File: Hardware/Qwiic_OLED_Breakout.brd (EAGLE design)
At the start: 27.3 x 29.7 mm, 45 parts, among them J1 QWIIC_RIGHT_ANGLE, J2 QWIIC_RIGHT_ANGLE

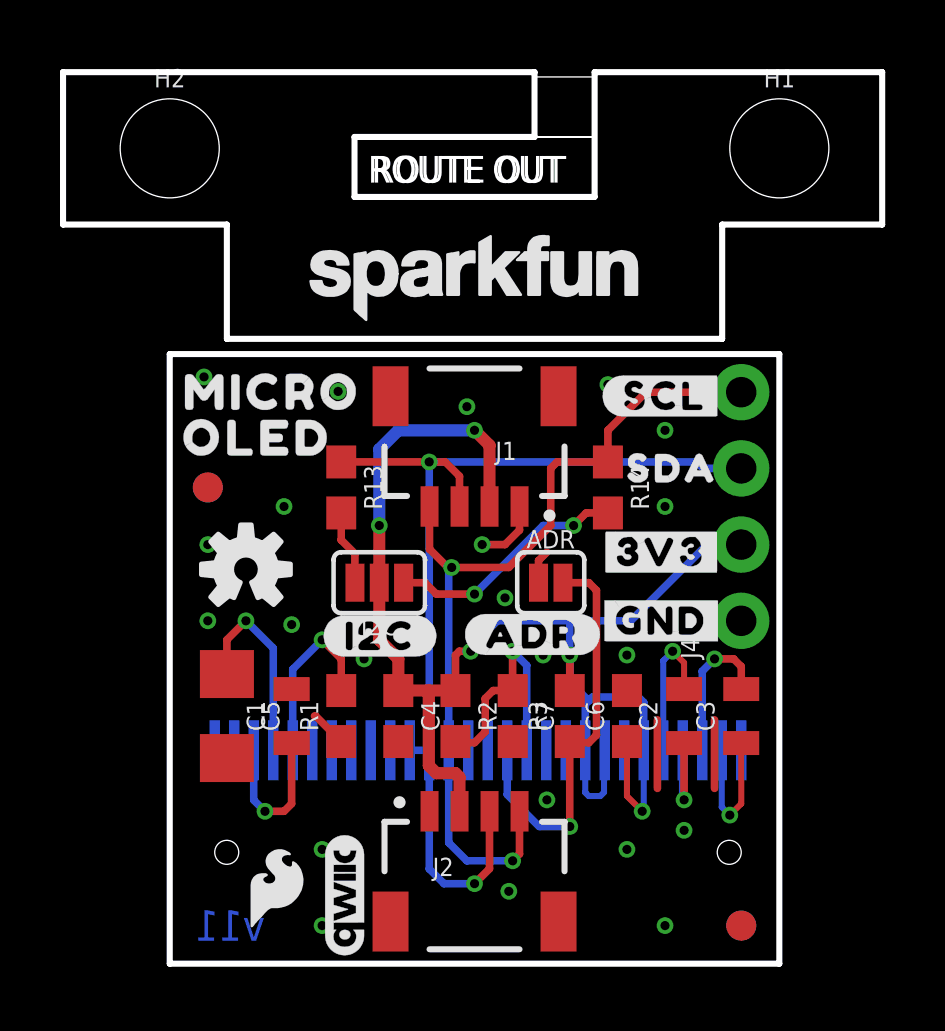
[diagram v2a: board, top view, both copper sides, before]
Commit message: Updates the isolate, replaces the main OLED part, adds some polygons
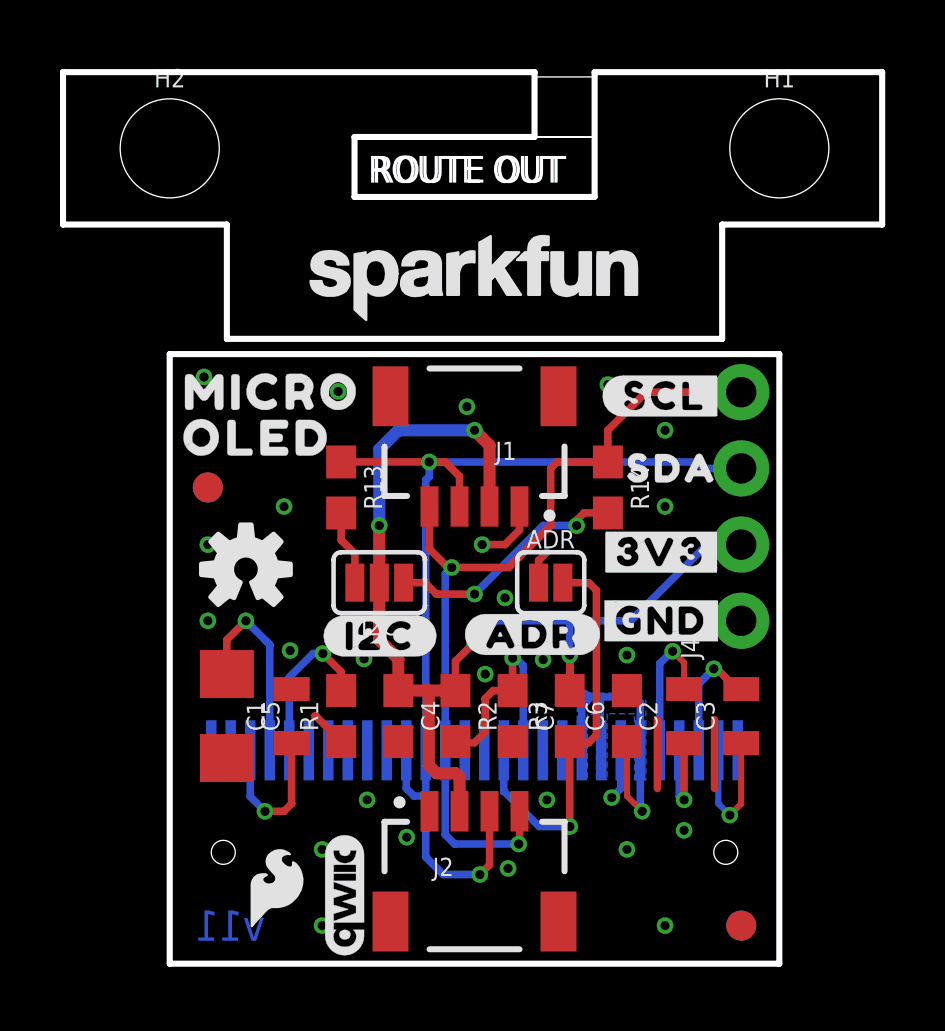
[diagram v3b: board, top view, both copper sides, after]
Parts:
- moved OLED1 8.89 mm to (10.2, 7.11)
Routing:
- net GND: track 9.18 -> 10.9 mm, vias 22 -> 26
- net D1/SDA/PICO: track 34.2 -> 35.2 mm
- net C2N: track 4.96 -> 4.12 mm
- net IREF: track 6.04 -> 5.37 mm
- net D0/SCL/SCK: track 29.6 -> 28.9 mm
- added copper zone on layer 16, net VDD

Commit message: Moves Ordering Instructions
* Updates notes in schematics
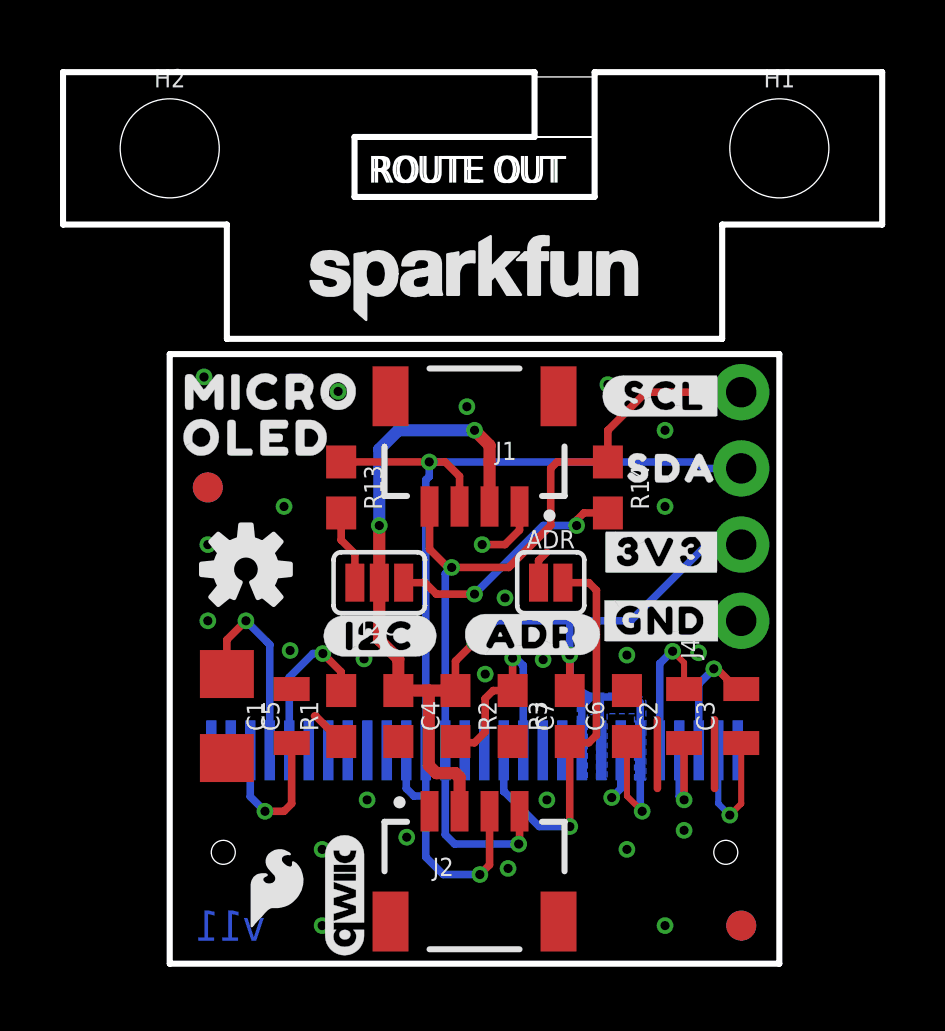
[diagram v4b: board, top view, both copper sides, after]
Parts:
- moved LOGO6 3.81 mm to (34.3, 47.0)
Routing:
- net GND: vias 26 -> 27
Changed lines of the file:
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@@
 <layer number="45" name="Holes" color="7" fill="1" visible="yes" active="yes"/>
 <layer number="46" name="Milling" color="3" fill="1" visible="no" active="yes"/>
-<layer number="47" name="Measures" color="7" fill="1" visible="no" active="yes"/>
+<layer number="47" name="Measures" color="7" fill="1" visible="yes" active="yes"/>
 <layer number="48" name="Document" color="7" fill="1" visible="no" active="yes"/>
 <layer number="49" name="Reference" color="13" fill="1" visible="yes" active="yes"/>
 <layer number="50" name="dxf" color="7" fill="1" visible="no" active="no"/>
 <layer number="51" name="tDocu" color="6" fill="1" visible="yes" active="yes"/>
-<layer number="52" name="bDocu" color="7" fill="1" visible="no" active="yes"/>
+<layer number="52" name="bDocu" color="7" fill="1" visible="yes" active="yes"/>
 <layer number="53" name="tGND_GNDA" color="7" fill="1" visible="no" active="no"/>
 <layer number="54" name="bGND_GNDA" color="7" fill="1" visible="no" active="no"/>
@@
 <dimension x1="10.16" y1="5.08" x2="0" y2="5.08" x3="5.08" y3="-5.08" textsize="1.778" textratio="12" layer="47" unit="inch"/>
 <text x="-26.67" y="-6.35" size="1.778" layer="47" font="vector" ratio="12">Units in Inches</text>
-<text x="31.75" y="34.29" size="1.778" layer="51" font="vector" ratio="12">Two Layer Board</text>
-<text x="31.75" y="31.75" size="1.778" layer="51" font="vector" ratio="12">Red Soldermask</text>
-<text x="31.75" y="29.21" size="1.778" layer="51" font="vector" ratio="12">White Silkscreen</text>
-<text x="31.75" y="26.67" size="1.778" layer="51" font="vector" ratio="12">1.6mm Thickness</text>
-<text x="31.75" y="24.13" size="1.778" layer="51" font="vector" ratio="12">Lead-Free HASL</text>
+<text x="35.56" y="34.29" size="1.778" layer="51" font="vector" ratio="12">Two Layer Board</text>
+<text x="35.56" y="31.75" size="1.778" layer="51" font="vector" ratio="12">Red Soldermask</text>
+<text x="35.56" y="29.21" size="1.778" layer="51" font="vector" ratio="12">White Silkscreen</text>
+<text x="35.56" y="26.67" size="1.778" layer="51" font="vector" ratio="12">1.6mm Thickness</text>
+<text x="35.56" y="24.13" size="1.778" layer="51" font="vector" ratio="12">Lead-Free HASL</text>
 <dimension x1="0" y1="27.178" x2="20.32" y2="27.178" x3="10.16" y3="34.29" textsize="1.778" textratio="15" layer="47" unit="inch"/>
 <dimension x1="20.32" y1="0" x2="20.32" y2="11.43" x3="26.67" y3="5.715" textsize="1.778" textratio="15" layer="47" unit="inch"/>
@@
 <element name="LOGO2" library="SparkFun-Aesthetics" package="SFE_LOGO_NAME_.1" value="SFE_LOGO_NAME.1_INCH" x="10.16" y="22.86" smashed="yes"/>
 <element name="LOGO4" library="SparkFun-Aesthetics" package="SFE_LOGO_NAME_.1" value="SFE_LOGO_NAME.1_INCH" x="6.604" y="18.415" smashed="yes" rot="MR0"/>
-<element name="LOGO6" library="SparkFun-Aesthetics" package="ORDERING_INSTRUCTIONS" value="SPECIAL_INSTRUCTIONS-ORDERING" x="30.48" y="46.99" smashed="yes"/>
+<element name="LOGO6" library="SparkFun-Aesthetics" package="ORDERING_INSTRUCTIONS" value="SPECIAL_INSTRUCTIONS-ORDERING" x="34.29" y="46.99" smashed="yes"/>
 <element name="U$15" library="SparkFun-Aesthetics" package="SFE_LOGO_FLAME_.1" value="" x="3.556" y="2.54" smashed="yes"/>
 <element name="J4" library="SparkFun-Connectors" package="1X04_NO_SILK" value="" x="19.05" y="11.43" smashed="yes" rot="R90">
@@
 <via x="7.8994" y="4.2164" extent="1-16" drill="0.3048"/>
 <via x="10.5156" y="9.652" extent="1-16" drill="0.3048"/>
+<via x="17.6276" y="10.3632" extent="1-16" drill="0.3048"/>
 </signal>
 <signal name="VDD">

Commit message: Adds a single via
* Gets judicious with the text in the schematic
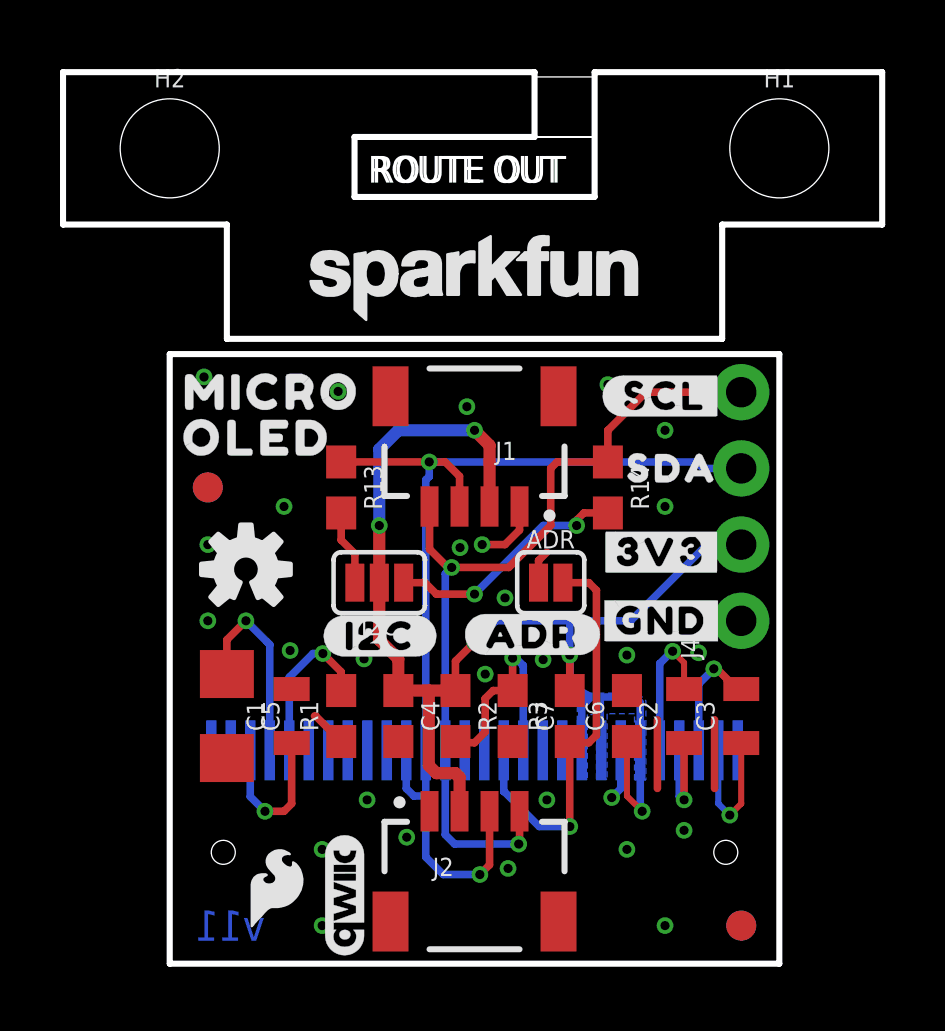
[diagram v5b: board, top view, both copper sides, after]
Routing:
- net GND: vias 27 -> 28
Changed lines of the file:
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@@
 <layer number="50" name="dxf" color="7" fill="1" visible="no" active="no"/>
 <layer number="51" name="tDocu" color="6" fill="1" visible="yes" active="yes"/>
-<layer number="52" name="bDocu" color="7" fill="1" visible="yes" active="yes"/>
+<layer number="52" name="bDocu" color="7" fill="1" visible="no" active="yes"/>
 <layer number="53" name="tGND_GNDA" color="7" fill="1" visible="no" active="no"/>
 <layer number="54" name="bGND_GNDA" color="7" fill="1" visible="no" active="no"/>
@@
 <via x="10.5156" y="9.652" extent="1-16" drill="0.3048"/>
 <via x="17.6276" y="10.3632" extent="1-16" drill="0.3048"/>
+<via x="9.6774" y="13.8684" extent="1-16" drill="0.3048"/>
 </signal>
 <signal name="VDD">
